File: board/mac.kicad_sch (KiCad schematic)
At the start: 1 part, among them U4 11AA02E48

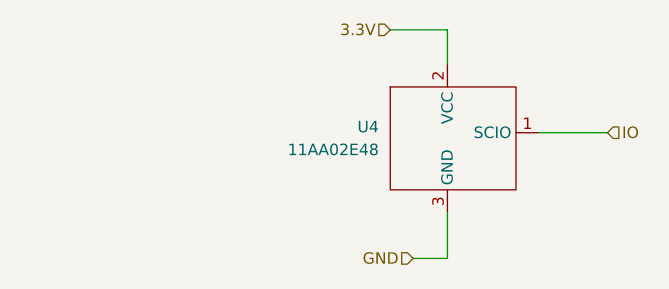
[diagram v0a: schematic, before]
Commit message: added needle addapter
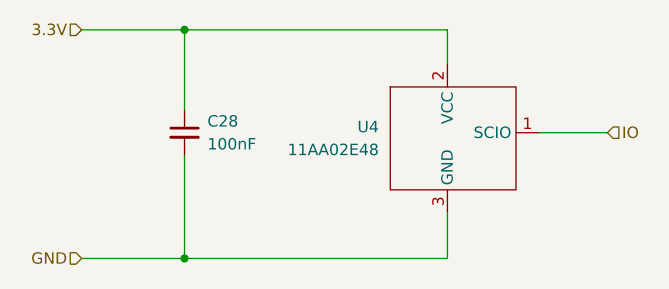
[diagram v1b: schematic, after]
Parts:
- added C28: 100nF, Capacitor_SMD:C_0603_1608Metric, symbol Device:C_Small
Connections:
- net 3.3V: now also C28.1
- net GND: now also C28.2
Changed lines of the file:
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@@
 (kicad_sch (version 20211123) (generator eeschema)
   (paper "A4")
+  (junction (at 78.74 120.65) (diameter 0) (color 0 0 0 0)
+  )
+  (junction (at 78.74 95.25) (diameter 0) (color 0 0 0 0)
+  )
   (wire (pts (xy 107.95 120.65) (xy 107.95 115.57))
+    (stroke (width 0) (type default) (color 0 0 0 0))
+  )
+  (wire (pts (xy 78.74 109.22) (xy 78.74 120.65))
+    (stroke (width 0) (type default) (color 0 0 0 0))
+  )
+  (wire (pts (xy 78.74 95.25) (xy 107.95 95.25))
+    (stroke (width 0) (type default) (color 0 0 0 0))
+  )
+  (wire (pts (xy 78.74 120.65) (xy 107.95 120.65))
+    (stroke (width 0) (type default) (color 0 0 0 0))
+  )
+  (wire (pts (xy 78.74 95.25) (xy 78.74 104.14))
     (stroke (width 0) (type default) (color 0 0 0 0))
   )
@@
     (stroke (width 0) (type default) (color 0 0 0 0))
   )
-  (wire (pts (xy 104.14 120.65) (xy 107.95 120.65))
+  (wire (pts (xy 67.31 120.65) (xy 78.74 120.65))
     (stroke (width 0) (type default) (color 0 0 0 0))
   )
@@
     (stroke (width 0) (type default) (color 0 0 0 0))
   )
-  (wire (pts (xy 101.6 95.25) (xy 107.95 95.25))
+  (wire (pts (xy 67.31 95.25) (xy 78.74 95.25))
     (stroke (width 0) (type default) (color 0 0 0 0))
   )
-  (hierarchical_label "GND" (shape input) (at 104.14 120.65 180)
+  (hierarchical_label "GND" (shape input) (at 67.31 120.65 180)
     (effects (font (size 1.27 1.27)) (justify right))
   )
@@
     (effects (font (size 1.27 1.27)) (justify left))
   )
-  (hierarchical_label "3.3V" (shape input) (at 101.6 95.25 180)
+  (hierarchical_label "3.3V" (shape input) (at 67.31 95.25 180)
     (effects (font (size 1.27 1.27)) (justify right))
   )
+  (symbol (lib_id "Device:C_Small") (at 78.74 106.68 0) (unit 1)
+    (in_bom yes) (on_board yes) (fields_autoplaced)
+    (property "Reference" "C28" (id 0) (at 81.28 105.4162 0)
+      (effects (font (size 1.27 1.27)) (justify left))
+    )
+    (property "Value" "100nF" (id 1) (at 81.28 107.9562 0)
+      (effects (font (size 1.27 1.27)) (justify left))
+    )
+    (property "Footprint" "Capacitor_SMD:C_0603_1608Metric" (id 2) (at 78.74 106.68 0)
+      (effects (font (size 1.27 1.27)) hide)
+    )
+    (property "Datasheet" "~" (id 3) (at 78.74 106.68 0)
+      (effects (font (size 1.27 1.27)) hide)
+    )
+    (pin "1")
+    (pin "2")
+  )
   (symbol (lib_id "parts:11AA02E48") (at 107.95 106.68 0) (unit 1)

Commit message: moved all components to top layer
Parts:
- C28: footprint Capacitor_SMD:C_0603_1608Metric -> Capacitor_SMD:C_0402_1005Metric
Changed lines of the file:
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@@
       (effects (font (size 1.27 1.27)) (justify left))
     )
-    (property "Footprint" "Capacitor_SMD:C_0603_1608Metric" (at 78.74 106.68 0)
+    (property "Footprint" "Capacitor_SMD:C_0402_1005Metric" (at 78.74 106.68 0)
       (effects (font (size 1.27 1.27)) hide)
     )

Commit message: added lcsc part numbers
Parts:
- C28: lcsc (none) -> C1525
- U4: lcsc (none) -> C616174
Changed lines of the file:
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@@
+      (effects (font (size 1.27 1.27)) hide)
+    )
+    (property "lcsc" "C1525" (at 78.74 106.68 0)
       (effects (font (size 1.27 1.27)) hide)
     )
@@
       (effects (font (size 1.27 1.27)) hide)
     )
+    (property "lcsc" "C616174" (at 107.95 106.68 0)
+      (effects (font (size 1.27 1.27)) hide)
+    )
